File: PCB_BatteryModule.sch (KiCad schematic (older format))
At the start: 47 parts, among them J1 Interconnect A, J2 Interconnect B, J3 Debug, J4 Conn_01x04, Q1 IRF7406, Q2 IRF7469, U1 LM22679, U2 ACS712, U3 XMC1404_F064, U4 TLE7251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

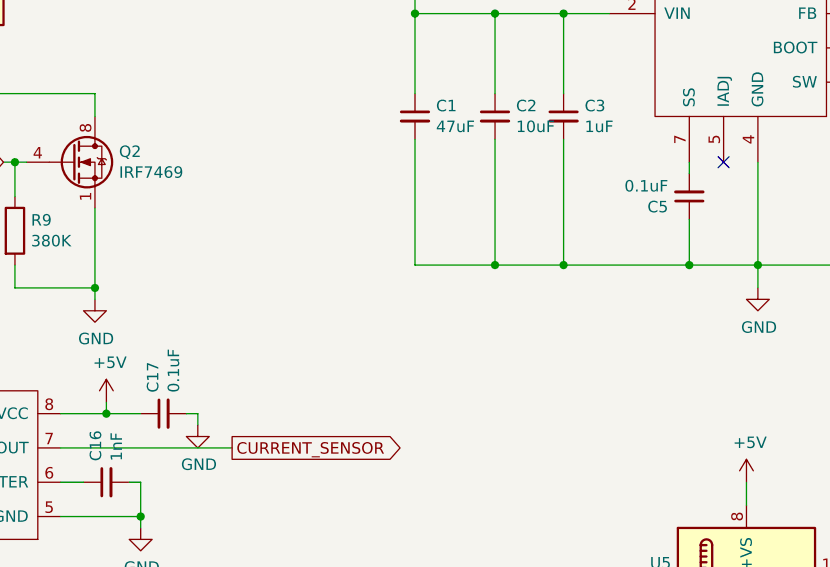
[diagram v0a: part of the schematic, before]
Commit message: Change the 0.1 uF capacitors to 100 nF which is the same
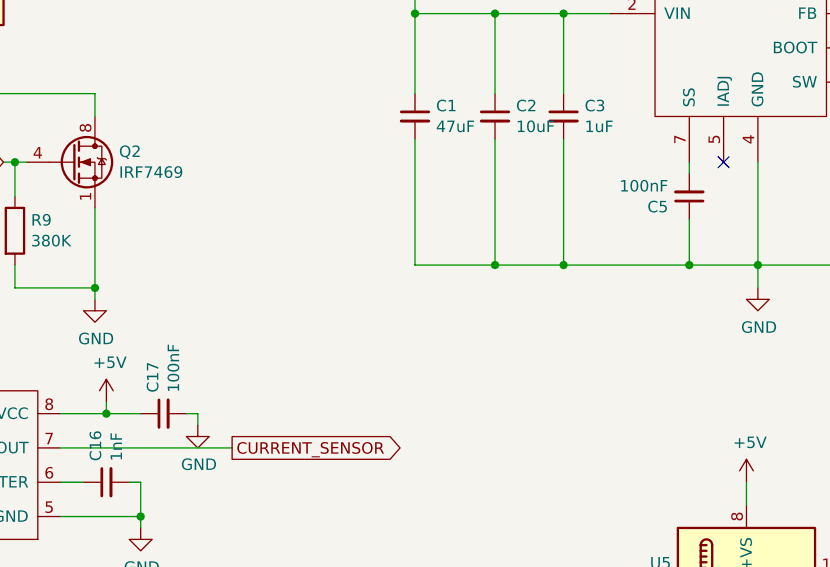
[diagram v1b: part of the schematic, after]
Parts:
- C17, C5: value 0.1uF -> 100nF
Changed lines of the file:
@@
 P 7450 1850
 F 0 "C5" H 7542 1896 50  0000 L CNN
-F 1 "0.1uF" H 7542 1805 50  0000 L CNN
+F 1 "100nF" H 7542 1805 50  0000 L CNN
 F 2 "PCB_BatteryModule:C_0805_HandSoldering" H 7450 1850 50  0001 C CNN
 F 3 "~" H 7450 1850 50  0001 C CNN
@@
 P 5150 2800
 F 0 "C17" H 5242 2846 50  0000 L CNN
-F 1 "0.1uF" H 5242 2755 50  0000 L CNN
+F 1 "100nF" H 5242 2755 50  0000 L CNN
 F 2 "PCB_BatteryModule:C_0805_HandSoldering" H 5150 2800 50  0001 C CNN
 F 3 "~" H 5150 2800 50  0001 C CNN

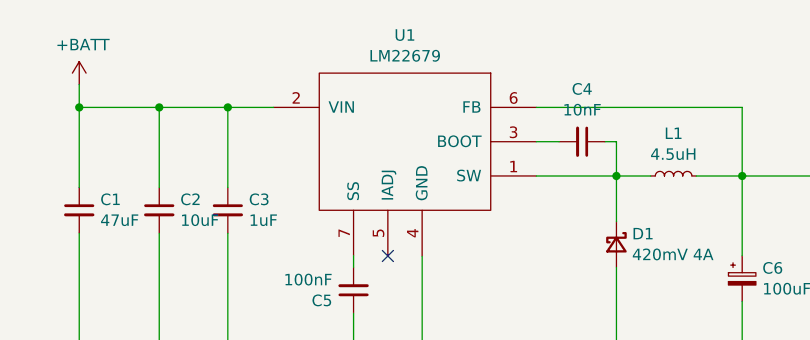
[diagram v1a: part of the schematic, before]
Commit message: Add the 5.0 suffix to the voltage regulator to make it more specific
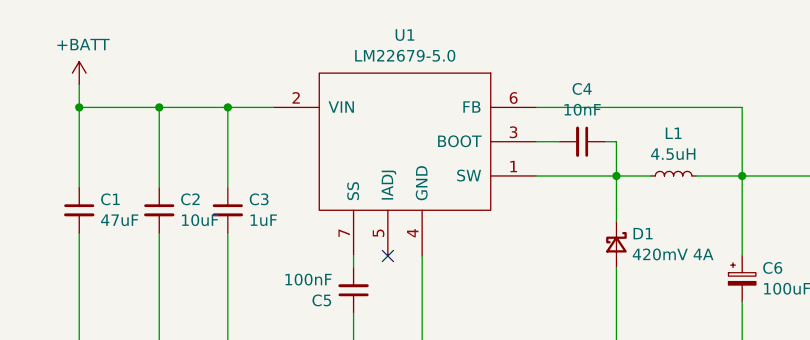
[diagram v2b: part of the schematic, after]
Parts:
- U1: value LM22679 -> LM22679-5.0
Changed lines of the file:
@@
 P 7650 900
 F 0 "U1" H 7675 1065 50  0000 C CNN
-F 1 "LM22679" H 7675 974 50  0000 C CNN
+F 1 "LM22679-5.0" H 7675 974 50  0000 C CNN
 F 2 "TO_SOT_Packages_SMD:TO-263-7_TabPin8" H 7650 900 50  0001 C CNN
 F 3 "" H 7650 900 50  0001 C CNN
